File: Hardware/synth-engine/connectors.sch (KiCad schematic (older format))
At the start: 1 part, among them J8 Conn_02x12_Odd_Even

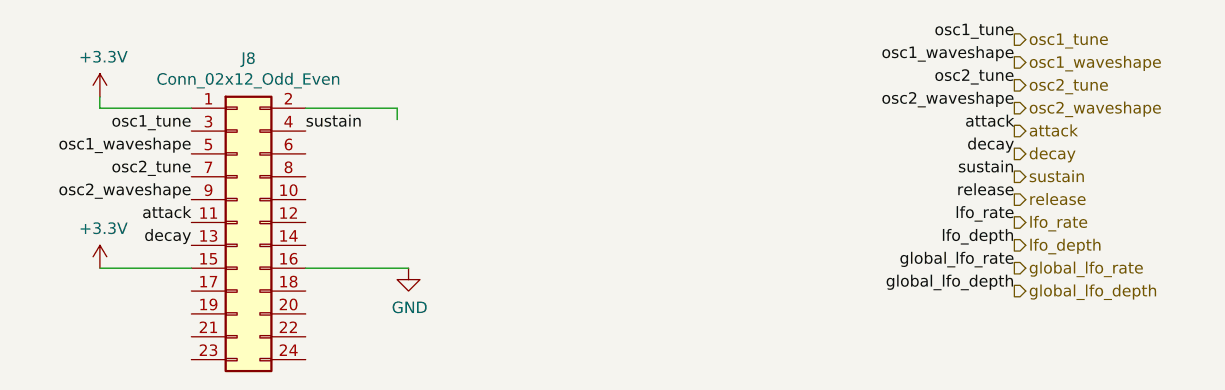
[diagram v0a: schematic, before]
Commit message: initial routing complete. Still need to do ground plane pours. There are still some issues with incorrect footprints.
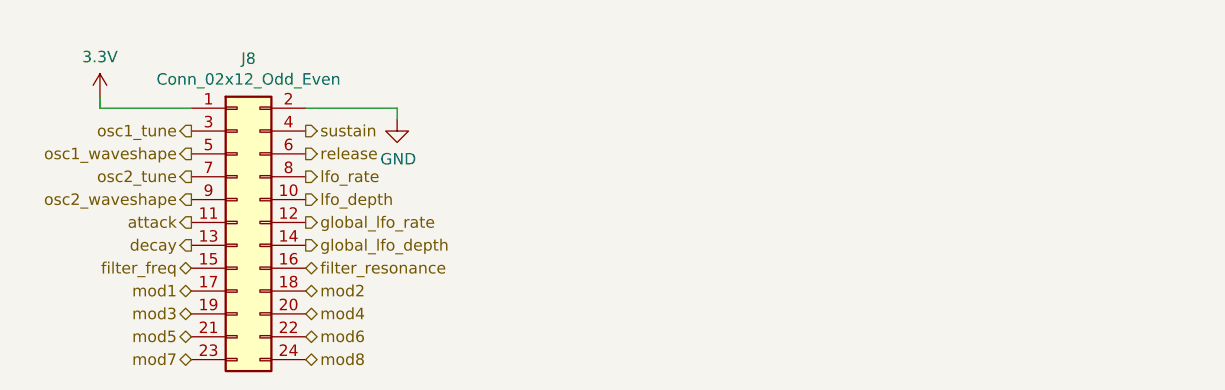
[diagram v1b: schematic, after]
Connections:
- net labels added: 3.3V, filter_freq, filter_resonance, mod1, mod2, mod3, mod4, mod5, mod6, mod7, mod8
- net labels removed: +3.3V
- wire segments 6 -> 4
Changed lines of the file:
@@
-	1    0    0    -1
-$EndComp
-Text Label 5350 3950 2    50   ~ 0
-attack
-Text Label 5350 4050 2    50   ~ 0
-decay
-Text Label 5850 3550 0    50   ~ 0
-sustain
-Text Label 8950 3850 2    50   ~ 0
-release
-Text Label 8950 3950 2    50   ~ 0
-lfo_rate
-Text Label 8950 4050 2    50   ~ 0
-lfo_depth
-Text Label 5350 3550 2    50   ~ 0
-osc1_tune
-Text Label 5350 3650 2    50   ~ 0
-osc1_waveshape
-Text Label 5350 3750 2    50   ~ 0
-osc2_tune
-Text Label 5350 3850 2    50   ~ 0
-osc2_waveshape
-$Comp
-L power:+3.3V #PWR0121
-U 1 1 5DDD170E
-P 4950 3400
-F 0 "#PWR0121" H 4950 3250 50  0001 C CNN
-F 1 "+3.3V" H 4965 3573 50  0000 C CNN
-F 2 "" H 4950 3400 50  0001 C CNN
-F 3 "" H 4950 3400 50  0001 C CNN
-	1    4950 3400
 	1    0    0    -1
 $EndComp
@@
 Wire Wire Line
 	6250 3450 5850 3450
+Text HLabel 5350 3550 0    50   Output ~ 0
+osc1_tune
+Text HLabel 5350 3650 0    50   Output ~ 0
+osc1_waveshape
+Text HLabel 5350 3750 0    50   Output ~ 0
+osc2_tune
+Text HLabel 5350 3850 0    50   Output ~ 0
+osc2_waveshape
+Text HLabel 5350 3950 0    50   Output ~ 0
+attack
+Text HLabel 5350 4050 0    50   Output ~ 0
+decay
+Text HLabel 5850 3550 2    50   Output ~ 0
+sustain
+Text HLabel 5850 3650 2    50   Output ~ 0
+release
+Text HLabel 5850 3750 2    50   Output ~ 0
+lfo_rate
+Text HLabel 5850 3850 2    50   Output ~ 0
+lfo_depth
+Text HLabel 5850 3950 2    50   Output ~ 0
+global_lfo_rate
+Text HLabel 5850 4050 2    50   Output ~ 0
+global_lfo_depth
+Text HLabel 5350 4150 0    50   BiDi ~ 0
+filter_freq
+Text HLabel 5850 4150 2    50   BiDi ~ 0
+filter_resonance
 $Comp
-L power:GND #PWR0123
-U 1 1 5DDD1795
-P 6300 4150
-F 0 "#PWR0123" H 6300 3900 50  0001 C CNN
-F 1 "GND" H 6305 3977 50  0000 C CNN
-F 2 "" H 6300 4150 50  0001 C CNN
-F 3 "" H 6300 4150 50  0001 C CNN
-	1    6300 4150
+L power:GND #PWR0122
+U 1 1 5DE076CA
+P 6250 3500
+F 0 "#PWR0122" H 6250 3250 50  0001 C CNN
+F 1 "GND" H 6255 3327 50  0000 C CNN
+F 2 "" H 6250 3500 50  0001 C CNN
+F 3 "" H 6250 3500 50  0001 C CNN
+	1    6250 3500
 	1    0    0    -1
 $EndComp
-Wire Wire Line
-	6300 4150 5850 4150
+Text HLabel 5350 4250 0    50   BiDi ~ 0
+mod1
+Text HLabel 5850 4250 2    50   BiDi ~ 0
+mod2
+Text HLabel 5350 4350 0    50   BiDi ~ 0
+mod3
+Text HLabel 5850 4350 2    50   BiDi ~ 0
+mod4
+Text HLabel 5350 4450 0    50   BiDi ~ 0
+mod5
+Text HLabel 5850 4450 2    50   BiDi ~ 0
+mod6
+Text HLabel 5350 4550 0    50   BiDi ~ 0
+mod7
+Text HLabel 5850 4550 2    50   BiDi ~ 0
+mod8
 $Comp
-L power:+3.3V #PWR0124
-U 1 1 5DDD17B1
-P 4950 4150
-F 0 "#PWR0124" H 4950 4000 50  0001 C CNN
-F 1 "+3.3V" H 4965 4323 50  0000 C CNN
-F 2 "" H 4950 4150 50  0001 C CNN
-F 3 "" H 4950 4150 50  0001 C CNN
-	1    4950 4150
+L SparkFun-Aesthetics:3.3V #SUPPLY0107
+U 1 1 5DE1F03B
+P 4950 3400
+F 0 "#SUPPLY0107" H 4950 3400 50  0001 L BNN
+F 1 "3.3V" H 4950 3574 50  0000 C CNN
+F 2 "" H 4950 3400 50  0001 C CNN
+F 3 "" H 4950 3400 50  0001 C CNN
+	1    4950 3400
 	1    0    0    -1
 $EndComp
-Wire Wire Line
-	4950 4150 5350 4150
-Text Label 8950 4150 2    50   ~ 0
-global_lfo_rate
-Text Label 8950 4250 2    50   ~ 0
-global_lfo_depth
-Text Label 8950 3550 2    50   ~ 0
-attack
-Text Label 8950 3650 2    50   ~ 0
-decay
-Text Label 8950 3150 2    50   ~ 0
-osc1_tune
-Text Label 8950 3250 2    50   ~ 0
-osc1_waveshape
-Text Label 8950 3350 2    50   ~ 0
-osc2_tune
-Text Label 8950 3450 2    50   ~ 0
-osc2_waveshape
-Text Label 8950 3750 2    50   ~ 0
-sustain
-Text HLabel 8950 3150 2    50   Output ~ 0
-osc1_tune
-Text HLabel 8950 3250 2    50   Output ~ 0
-osc1_waveshape
-Text HLabel 8950 3350 2    50   Output ~ 0
-osc2_tune
-Text HLabel 8950 3450 2    50   Output ~ 0
-osc2_waveshape
-Text HLabel 8950 3550 2    50   Output ~ 0
-attack
-Text HLabel 8950 3650 2    50   Output ~ 0
-decay
-Text HLabel 8950 3750 2    50   Output ~ 0
-sustain
-Text HLabel 8950 3850 2    50   Output ~ 0
-release
-Text HLabel 8950 3950 2    50   Output ~ 0
-lfo_rate
-Text HLabel 8950 4050 2    50   Output ~ 0
-lfo_depth
-Text HLabel 8950 4150 2    50   Output ~ 0
-global_lfo_rate
-Text HLabel 8950 4250 2    50   Output ~ 0
-global_lfo_depth
 $EndSCHEMATC
